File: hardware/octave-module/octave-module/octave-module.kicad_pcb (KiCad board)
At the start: 2 copper layers, 164.5 x 12 mm, 26 parts, among them J1 JST_SH_4P, J2 JST_SH_4P

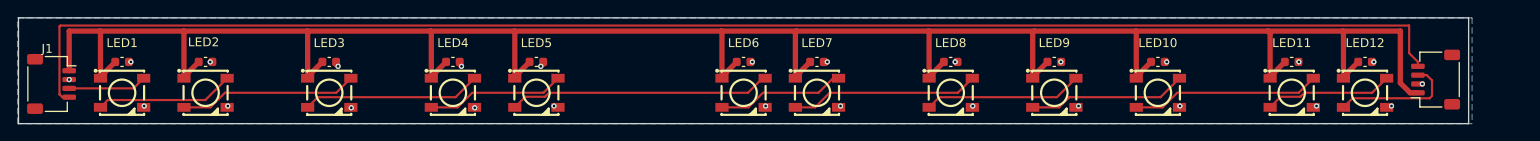
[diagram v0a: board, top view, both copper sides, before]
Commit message: Add octave-module flex PCB (fab-ready) + hardware to main
octave-module: uniform 13.708 mm LED pitch (caps aligned), solder lap-seam (J2 output / J3 input pads) with J2 plated 0.8 mm solder-access holes, full routing + GND pour, J1 placement; seam-lap footprint library; spacing/seam design docs; regenerated BOM + production files (J1 DNP, caps C14663, LEDs C2761795). Also controller_v2 + hardware BOM/docs.

Co-Authored-By: Claude Opus 4.8 <noreply@anthropic.com>
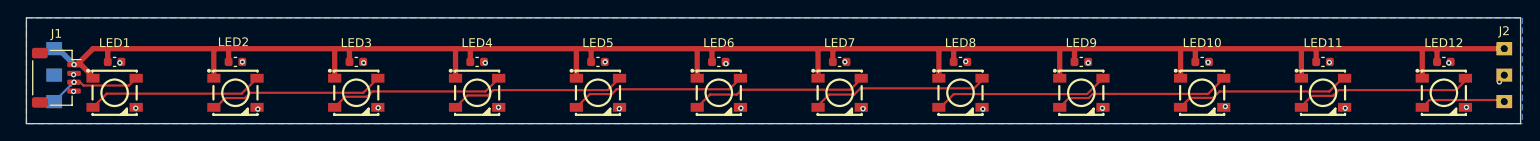
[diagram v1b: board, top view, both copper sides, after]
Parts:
- added J3: Conn_01x03, seam-lap:Seam_LapPad_IN_1x03, B.Cu at (55.3, 49.5)
- J1: value JST_SH_4P -> Conn_01x04_Socket
- J2: value JST_SH_4P -> Conn_01x03; footprint Connector_JST:JST_SH_SM04B-SRSS-TB_1x04-1MP_P1.00mm_Horizontal -> seam-lap:Seam_LapPad_OUT_1x03
- moved C12 8.94 mm to (212.9, 48.0)
- moved LED12 8.94 mm to (212.9, 51.5)
- moved J2 7.81 mm to (219.8, 49.5), turned to 0 degrees
- moved C5 6.98 mm to (117.0, 48.0)
- moved LED5 6.98 mm to (117.0, 51.5)
- moved C10 5.02 mm to (185.5, 48.0)
- moved LED10 5.02 mm to (185.5, 51.5)
- moved C11 3.55 mm to (199.2, 48.0)
- moved LED11 3.55 mm to (199.2, 51.5)
- moved C2 3.39 mm to (75.9, 48.0)
- moved LED2 3.39 mm to (75.9, 51.5)
- moved C3 3.07 mm to (89.6, 48.0)
- moved LED3 3.07 mm to (89.6, 51.5)
- moved C9 3.07 mm to (171.8, 48.0)
- moved LED9 3.07 mm to (171.8, 51.5)
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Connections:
- J1 pad 4: /DIN_PASS -> GND
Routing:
- net /DIN_PASS: track 167.1 -> 0.00 mm
- net +5V: track 259.0 -> 224.3 mm, vias 0 -> 1
- net Net-(LED5-DOUT): track 30.0 -> 20.0 mm
- net Net-(LED11-DOUT): track 15.0 -> 20.2 mm
- net Net-(LED6-DOUT): track 15.1 -> 20.0 mm
- net /DOUT_OUT: track 14.3 -> 9.72 mm
- net Net-(LED4-DOUT): track 16.0 -> 20.0 mm
- net Net-(LED1-DOUT): track 16.1 -> 20.0 mm
- net Net-(LED10-DOUT): track 21.7 -> 20.0 mm
- net /DIN_IN: track 9.10 -> 10.7 mm, vias 0 -> 1
- net Net-(LED7-DOUT): track 21.7 -> 20.2 mm
- net Net-(LED10-DIN): track 18.5 -> 20.0 mm
- net Net-(LED8-DOUT): track 18.5 -> 20.0 mm
- net GND: track 6.87 -> 5.76 mm, vias 26 -> 27
- net Net-(LED3-DOUT): track 20.6 -> 20.0 mm
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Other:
- board size 164.5 x 12 mm -> 169.5 x 12 mm
